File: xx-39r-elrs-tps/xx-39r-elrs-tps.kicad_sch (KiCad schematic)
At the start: 47 parts, among them J1 SENSE, J10 PA2, J11 PWR1, J12 PWR2, J13 R_VCC, J14 GND1, J15 GND2, J16 GND3, J2 BAT, J3 M_PORT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

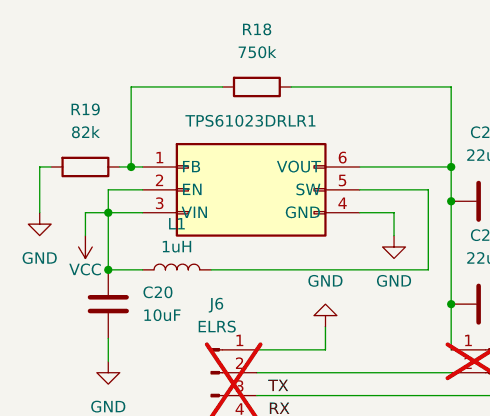
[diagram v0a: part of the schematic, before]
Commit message: Change R19 to 100K
With the 82K we were ending up with 5.8V boosted output, which made
the TPS cook itself. This now lowers it to a safe 5.2V with what I
have at hand (should be closer to 5V).
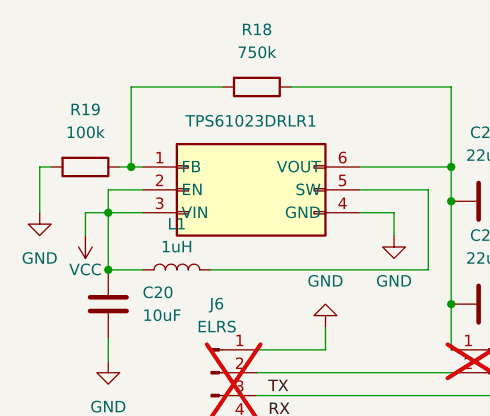
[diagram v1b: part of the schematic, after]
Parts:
- R19: value 82k -> 100k
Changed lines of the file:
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@@
 			)
 		)
-		(property "Value" "82k"
+		(property "Value" "100k"
 			(at 20.32 45.72 90)
 			(show_name no)
